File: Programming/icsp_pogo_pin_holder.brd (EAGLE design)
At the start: 17.8 x 15.2 mm, 4 parts

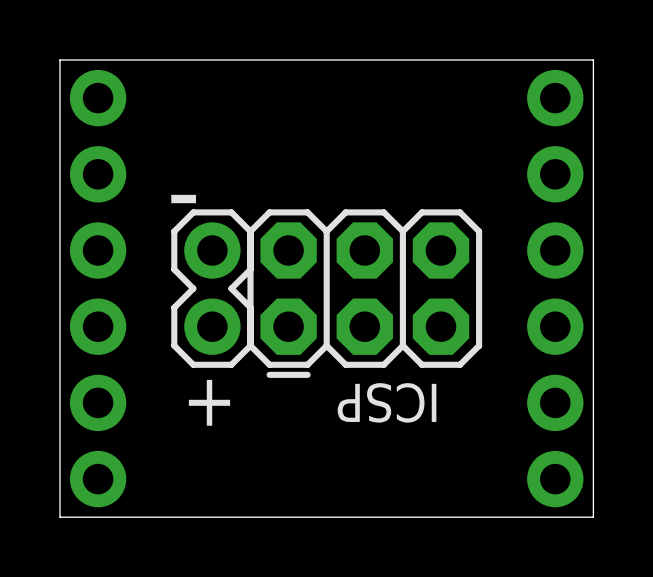
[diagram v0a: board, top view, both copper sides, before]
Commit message: increased pogo pin hole size in icsp header
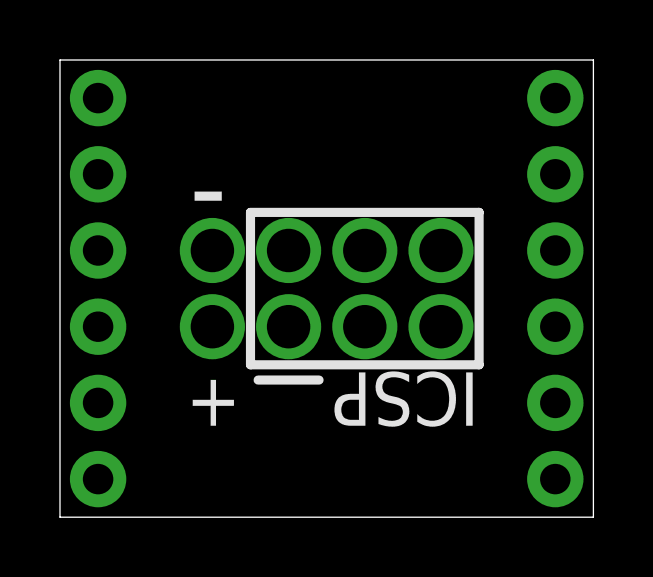
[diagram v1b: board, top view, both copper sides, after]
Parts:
- removed ICSP: AVR_SPI_PRG_6PTH, SparkFun-Connectors:2X3
- removed JP4: (no value), SparkFun-Connectors:1X02
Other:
- board text added: "02/24/2016 v1.1"
- board text added: "ICSP"
- board text removed: "02/02/2016 v1.0"
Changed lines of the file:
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@@
 <wire x1="17.78" y1="15.24" x2="0" y2="15.24" width="0" layer="20"/>
 <wire x1="0" y1="15.24" x2="0" y2="0" width="0" layer="20"/>
-<text x="4.064" y="4.826" size="1.778" layer="21" rot="MR180">+</text>
-<text x="3.556" y="12.192" size="2.54" layer="21" rot="MR180">-</text>
+<text x="4.191" y="4.826" size="1.778" layer="21" rot="MR180">+</text>
+<text x="4.318" y="12.446" size="2.794" layer="21" rot="MR180">-</text>
 <text x="5.334" y="4.572" size="0.9144" layer="22" rot="SMR180">awqua
 ICSP adapter
 for pogo pins</text>
-<text x="5.588" y="13.97" size="0.9144" layer="22" rot="SMR180">02/02/2016
-v1.0</text>
+<text x="5.588" y="13.97" size="0.9144" layer="22" rot="SMR180">02/24/2016
+v1.1</text>
+<text x="13.97" y="4.826" size="1.778" layer="21" rot="SR180">ICSP</text>
+<wire x1="6.35" y1="10.16" x2="6.35" y2="5.08" width="0.3048" layer="21"/>
+<wire x1="6.35" y1="5.08" x2="13.97" y2="5.08" width="0.3048" layer="21"/>
+<wire x1="13.97" y1="5.08" x2="13.97" y2="10.16" width="0.3048" layer="21"/>
+<wire x1="13.97" y1="10.16" x2="6.35" y2="10.16" width="0.3048" layer="21"/>
+<wire x1="6.604" y1="4.572" x2="8.636" y2="4.572" width="0.3048" layer="21"/>
 </plain>
 <attributes>
@@
 </autorouter>
 <elements>
-<element name="ICSP" library="SparkFun-Connectors" package="2X3" value="AVR_SPI_PRG_6PTH" x="7.62" y="6.35" smashed="yes">
-<attribute name="NAME" x="12.7" y="4.445" size="1.27" layer="25" ratio="10" rot="SR180"/>
-</element>
 <element name="JP2" library="SparkFun-Connectors" package="1X06_NO_SILK" value="" x="1.27" y="1.27" smashed="yes" rot="R90">
 <attribute name="PROD_ID" value="CONN-08437" x="1.27" y="1.27" size="1.778" layer="27" rot="R90" display="off"/>
@@
 <attribute name="VALUE" x="19.685" y="0" size="1.27" layer="27" rot="R90"/>
 </element>
-<element name="JP4" library="SparkFun-Connectors" package="1X02" value="" x="5.08" y="6.35" smashed="yes" rot="R90">
-<attribute name="VALUE" x="8.255" y="5.08" size="1.27" layer="27" rot="R90"/>
-</element>
 </elements>
 <signals>
+<signal name="N$1">
+<via x="5.08" y="8.89" extent="1-16" drill="1.4478" shape="octagon"/>
+<via x="7.62" y="8.89" extent="1-16" drill="1.4478" shape="octagon"/>
+<via x="7.62" y="6.35" extent="1-16" drill="1.4478" shape="octagon"/>
+<via x="10.16" y="6.35" extent="1-16" drill="1.4478" shape="octagon"/>
+<via x="10.16" y="8.89" extent="1-16" drill="1.4478" shape="octagon"/>
+<via x="12.7" y="8.89" extent="1-16" drill="1.4478" shape="octagon"/>
+<via x="12.7" y="6.35" extent="1-16" drill="1.4478" shape="octagon"/>
+<via x="5.08" y="6.35" extent="1-16" drill="1.4478" shape="octagon"/>
+</signal>
 </signals>
 </board>
